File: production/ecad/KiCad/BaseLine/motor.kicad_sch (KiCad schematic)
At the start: 20 parts, among them J1 VibeMotorConnector_1, J8 VibeMotorConnector_2, U1 DRV8830DGQR, U10 DRV8830DGQR

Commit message: footprint stuff
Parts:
- R53, R54: value R_US -> 10k
- TP23, TP24: footprint TestPoint:TestPoint_2Pads_Pitch2.54mm_Drill0.8mm -> (none)
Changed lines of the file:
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@@
 			)
 		)
-		(property "Footprint" "TestPoint:TestPoint_2Pads_Pitch2.54mm_Drill0.8mm"
+		(property "Footprint" ""
 			(at 264.16 48.26 0)
 			(effects
@@
 			)
 		)
-		(property "Footprint" "TestPoint:TestPoint_2Pads_Pitch2.54mm_Drill0.8mm"
+		(property "Footprint" ""
 			(at 264.16 110.49 0)
 			(effects
@@
 			)
 		)
-		(property "Value" "R_US"
+		(property "Value" "10k"
 			(at 219.71 101.6 90)
 			(effects
@@
 			)
 		)
-		(property "Value" "R_US"
+		(property "Value" "10k"
 			(at 218.44 39.37 90)
 			(effects

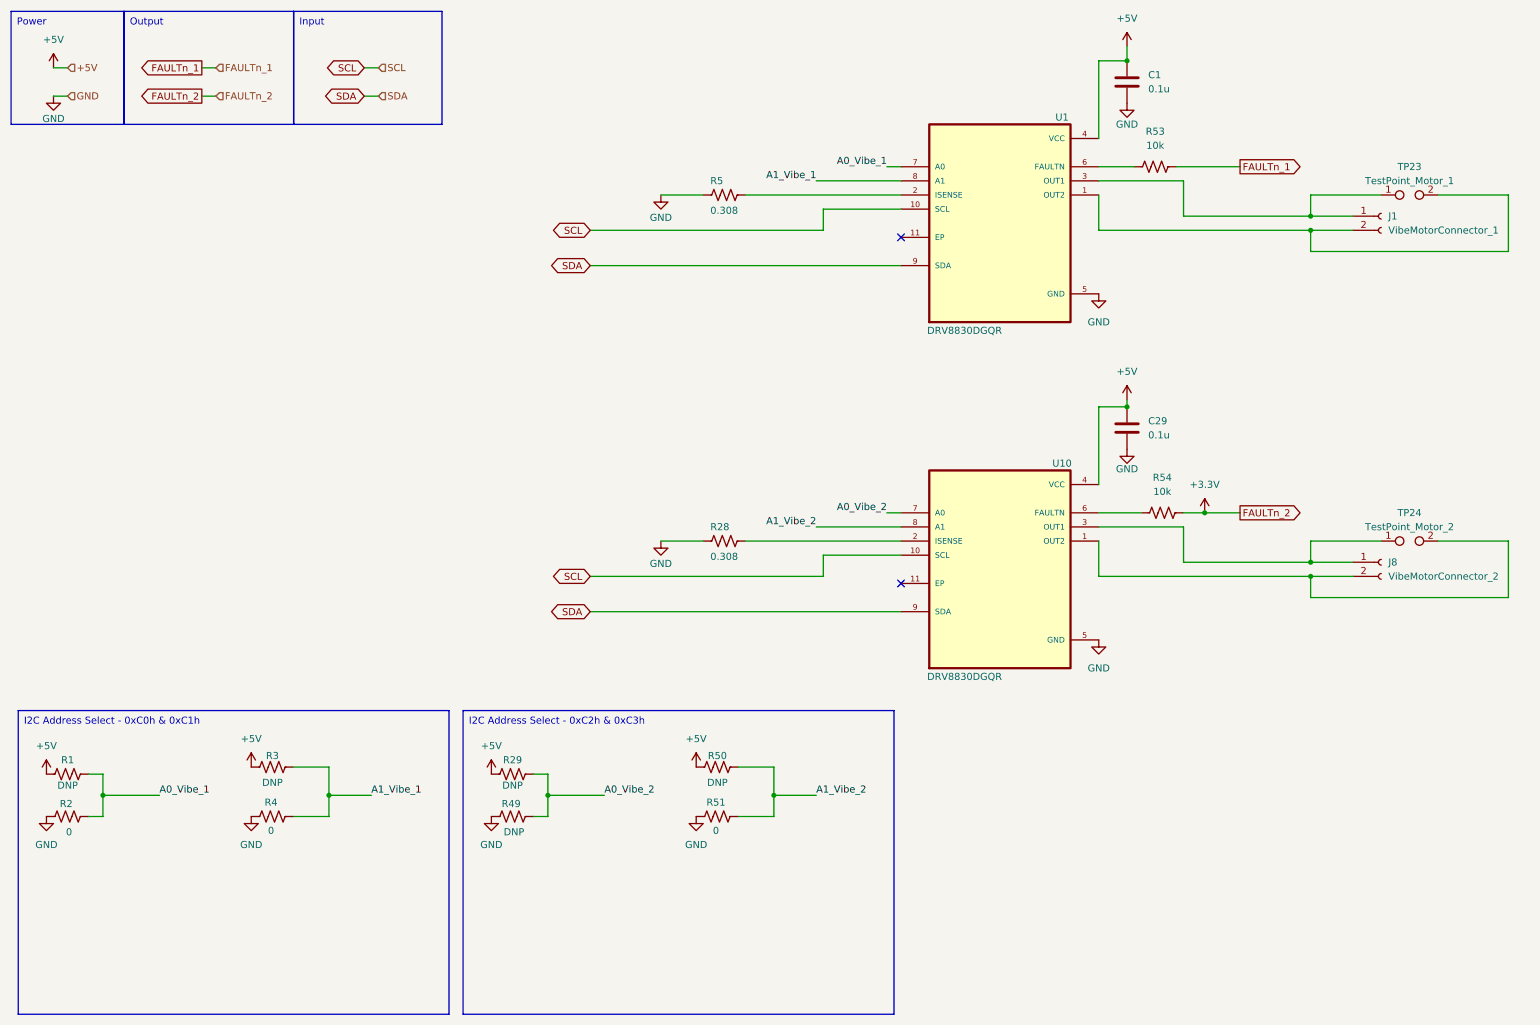
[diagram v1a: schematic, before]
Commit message: Connectors and heirarchal labels
added connectors for power on the Loadcell schem and the battery schem

added the MCU heirarchal labels
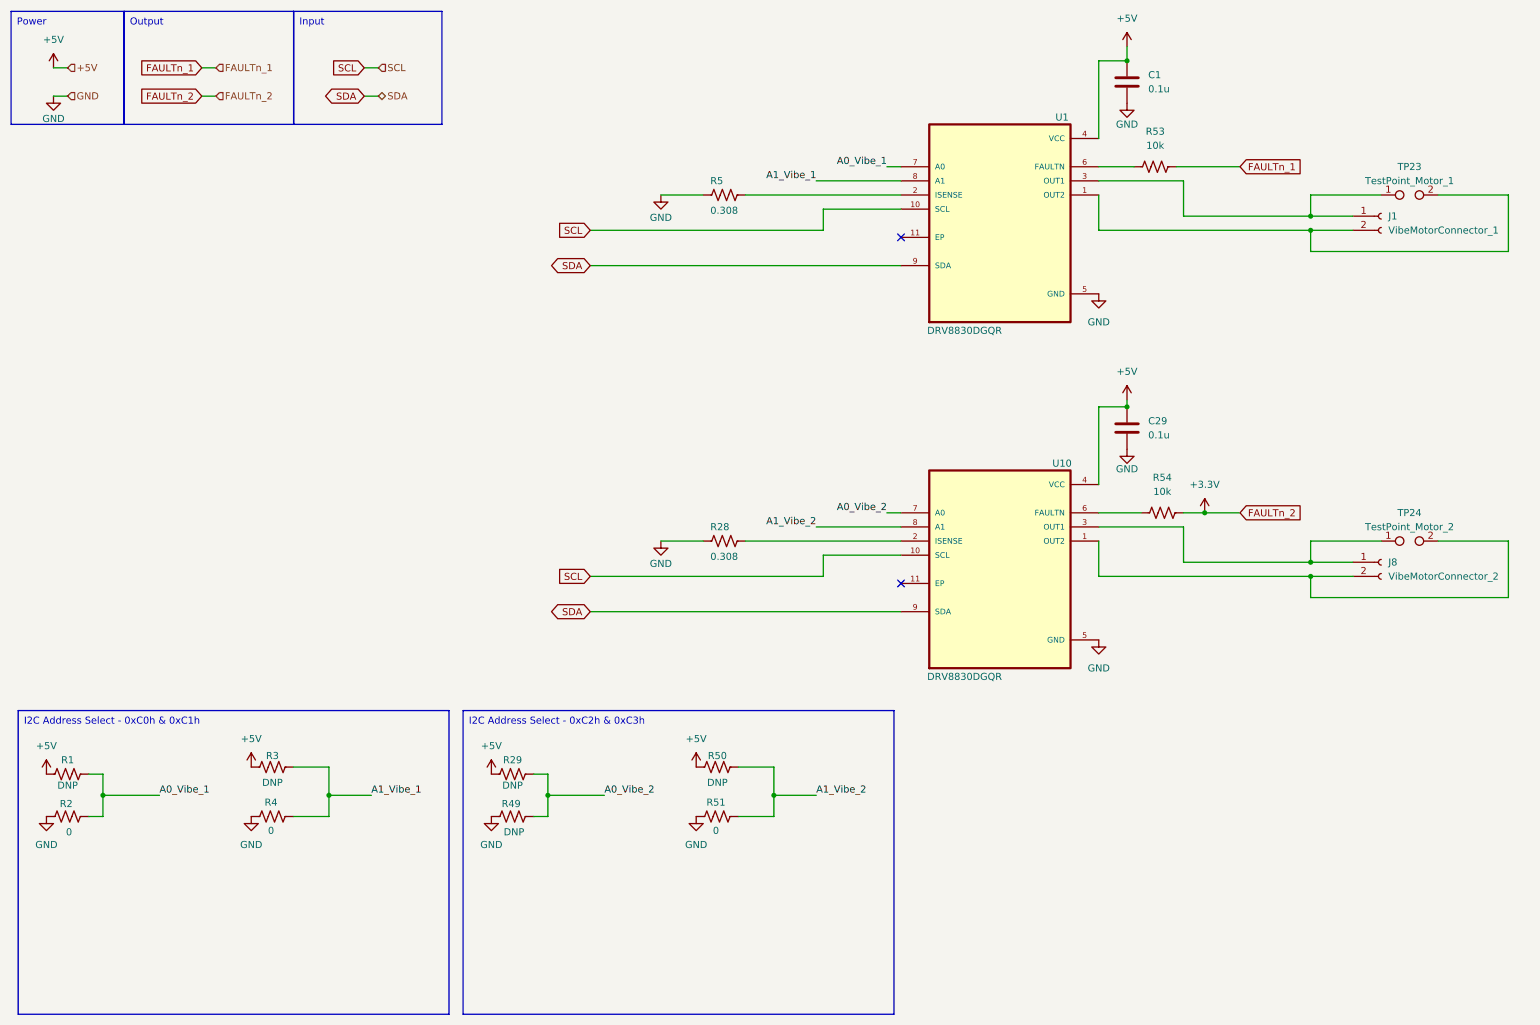
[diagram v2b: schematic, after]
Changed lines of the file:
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@@
 	)
 	(global_label "FAULTn_2"
-		(shape output)
+		(shape input)
 		(at 46.99 30.48 180)
 		(fields_autoplaced yes)
@@
 	)
 	(global_label "FAULTn_1"
-		(shape output)
+		(shape input)
 		(at 233.68 43.18 0)
 		(fields_autoplaced yes)
@@
 	)
 	(global_label "FAULTn_2"
-		(shape output)
+		(shape input)
 		(at 233.68 105.41 0)
 		(fields_autoplaced yes)
@@
 	)
 	(global_label "FAULTn_1"
-		(shape output)
+		(shape input)
 		(at 46.99 25.4 180)
 		(fields_autoplaced yes)
@@
 	)
 	(global_label "SCL"
-		(shape bidirectional)
+		(shape input)
 		(at 116.84 116.84 180)
 		(fields_autoplaced yes)
@@
 		)
 		(property "Intersheetrefs" "${INTERSHEET_REFS}"
-			(at 109.2359 116.84 0)
+			(at 110.3472 116.84 0)
 			(effects
 				(font
@@
 	)
 	(global_label "SCL"
-		(shape bidirectional)
+		(shape input)
 		(at 76.2 25.4 180)
 		(fields_autoplaced yes)
@@
 		)
 		(property "Intersheetrefs" "${INTERSHEET_REFS}"
-			(at 68.5959 25.4 0)
+			(at 69.7072 25.4 0)
 			(effects
 				(font
@@
 	)
 	(global_label "SCL"
-		(shape bidirectional)
+		(shape input)
 		(at 116.84 54.61 180)
 		(fields_autoplaced yes)
@@
 		)
 		(property "Intersheetrefs" "${INTERSHEET_REFS}"
-			(at 109.2359 54.61 0)
+			(at 110.3472 54.61 0)
 			(effects
 				(font
@@
 	)
 	(hierarchical_label "SDA"
-		(shape input)
+		(shape bidirectional)
 		(at 78.74 30.48 0)
 		(fields_autoplaced yes)

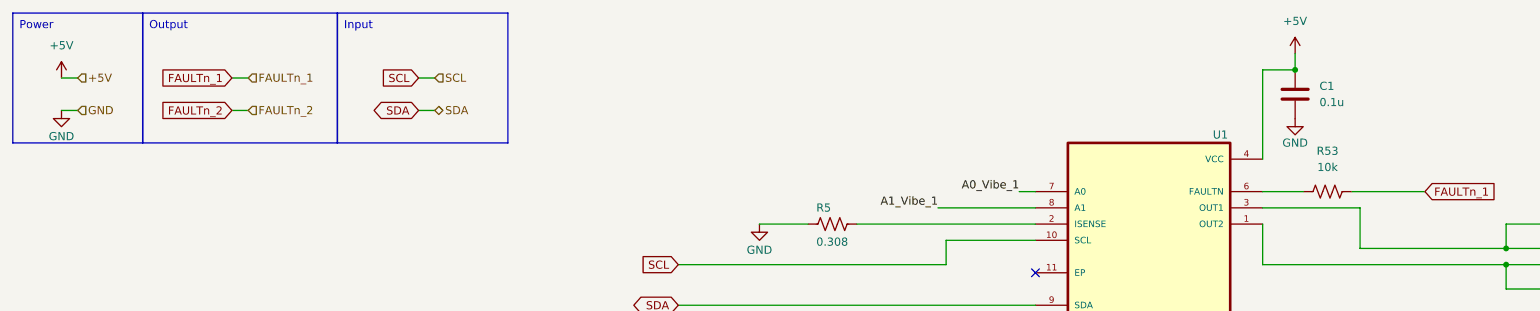
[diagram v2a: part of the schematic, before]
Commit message: fixed Faultn pull up to 3.3V
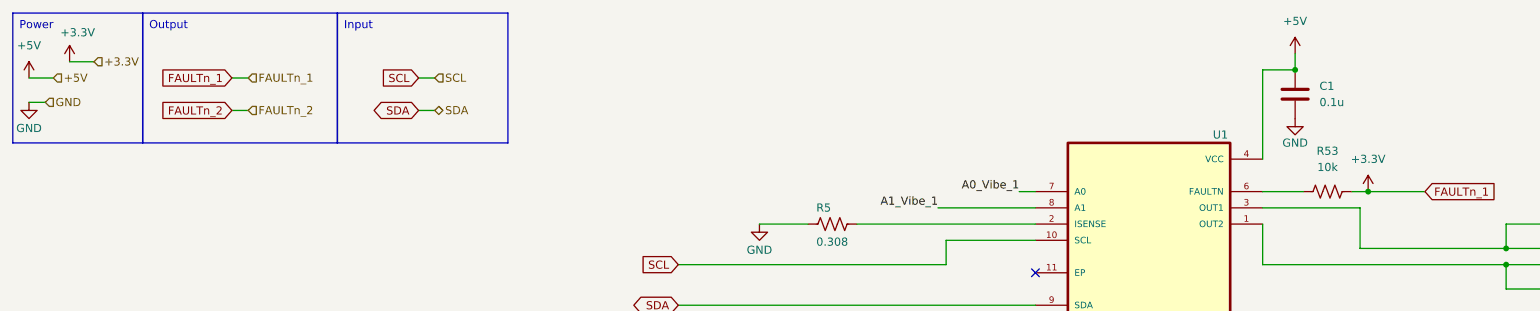
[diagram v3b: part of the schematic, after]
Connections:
- net FAULTn_1 is gone; now on net +3.3V: R53.2
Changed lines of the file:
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@@
 	)
 	(junction
+		(at 224.79 43.18)
+		(diameter 0)
+		(color 0 0 0 0)
+	)
+	(junction
 		(at 213.36 24.13)
 		(diameter 0)
@@
 	(wire
 		(pts
+			(xy 21.59 22.86) (xy 25.4 22.86)
+		)
+		(stroke
+			(width 0)
+			(type default)
+		)
+	)
+	(wire
+		(pts
 			(xy 109.22 152.4) (xy 106.68 152.4)
 		)
@@
 	(wire
 		(pts
-			(xy 20.32 25.4) (xy 22.86 25.4)
+			(xy 15.24 25.4) (xy 19.05 25.4)
 		)
 		(stroke
@@
 	(wire
 		(pts
+			(xy 224.79 43.18) (xy 233.68 43.18)
+		)
+		(stroke
+			(width 0)
+			(type default)
+		)
+	)
+	(wire
+		(pts
 			(xy 106.68 160.02) (xy 109.22 160.02)
 		)
@@
 	(wire
 		(pts
-			(xy 20.32 30.48) (xy 22.86 30.48)
+			(xy 15.24 29.21) (xy 17.78 29.21)
 		)
 		(stroke
@@
 	(wire
 		(pts
-			(xy 222.25 43.18) (xy 233.68 43.18)
+			(xy 222.25 43.18) (xy 224.79 43.18)
 		)
 		(stroke
@@
 	(hierarchical_label "GND"
 		(shape input)
-		(at 22.86 30.48 0)
+		(at 17.78 29.21 0)
 		(fields_autoplaced yes)
 		(effects
@@
 	(hierarchical_label "+5V"
 		(shape input)
-		(at 22.86 25.4 0)
+		(at 19.05 25.4 0)
+		(fields_autoplaced yes)
+		(effects
+			(font
+				(size 1.27 1.27)
+			)
+			(justify left)
+		)
+	)
+	(hierarchical_label "+3.3V"
+		(shape input)
+		(at 25.4 22.86 0)
 		(fields_autoplaced yes)
 		(effects
@@
 	(symbol
 		(lib_id "power:GND")
-		(at 20.32 30.48 0)
+		(at 15.24 29.21 0)
 		(unit 1)
 		(exclude_from_sim no)
@@
 		(dnp no)
 		(property "Reference" "#PWR092"
-			(at 20.32 36.83 0)
+			(at 15.24 35.56 0)
 			(effects
 				(font
@@
 		)
 		(property "Value" "GND"
-			(at 20.32 34.544 0)
+			(at 15.24 33.274 0)
 			(effects
 				(font
@@
 		)
 		(property "Footprint" ""
-			(at 20.32 30.48 0)
+			(at 15.24 29.21 0)
 			(effects
 				(font
@@
 		)
 		(property "Datasheet" ""
-			(at 20.32 30.48 0)
+			(at 15.24 29.21 0)
 			(effects
 				(font
@@
 		)
 		(property "Description" "Power symbol creates a global label with name \"GND\" , ground"
-			(at 20.32 30.48 0)
+			(at 15.24 29.21 0)
 			(effects
 				(font
@@
 	(symbol
 		(lib_id "power:+5V")
-		(at 20.32 25.4 0)
+		(at 15.24 25.4 0)
 		(unit 1)
 		(exclude_from_sim no)
@@
 		(fields_autoplaced yes)
 		(property "Reference" "#PWR091"
-			(at 20.32 29.21 0)
+			(at 15.24 29.21 0)
 			(effects
 				(font
@@
 		)
 		(property "Value" "+5V"
-			(at 20.32 20.32 0)
+			(at 15.24 20.32 0)
 			(effects
 				(font
@@
 		)
 		(property "Footprint" ""
-			(at 20.32 25.4 0)
+			(at 15.24 25.4 0)
 			(effects
 				(font
@@
 		)
 		(property "Datasheet" ""
-			(at 20.32 25.4 0)
+			(at 15.24 25.4 0)
 			(effects
 				(font
@@
 		)
 		(property "Description" "Power symbol creates a global label with name \"+5V\""
-			(at 20.32 25.4 0)
+			(at 15.24 25.4 0)
 			(effects
 				(font
@@
 	)
 	(symbol
+		(lib_id "power:+3.3V")
+		(at 224.79 43.18 0)
+		(unit 1)
+		(exclude_from_sim no)
+		(in_bom yes)
+		(on_board yes)
+		(dnp no)
+		(fields_autoplaced yes)
+		(property "Reference" "#PWR0121"
+			(at 224.79 46.99 0)
+			(effects
+				(font
+					(size 1.27 1.27)
+				)
+				(hide yes)
+			)
+		)
+		(property "Value" "+3.3V"
+			(at 224.79 38.1 0)
+			(effects
+				(font
+					(size 1.27 1.27)
+				)
+			)
+		)
+		(property "Footprint" ""
+			(at 224.79 43.18 0)
+			(effects
+				(font
+					(size 1.27 1.27)
+				)
+				(hide yes)
+			)
+		)
+		(property "Datasheet" ""
+			(at 224.79 43.18 0)
+			(effects
+				(font
+					(size 1.27 1.27)
+				)
+				(hide yes)
+			)
+		)
+		(property "Description" "Power symbol creates a global label with name \"+3.3V\""
+			(at 224.79 43.18 0)
+			(effects
+				(font
+					(size 1.27 1.27)
+				)
+				(hide yes)
+			)
+		)
+		(pin "1"
+		)
+		(instances
+			(project "BaseLine"
+				(path "/ba9eda21-3882-41e1-8265-3d8ac781da20/32bcaf69-2ff4-46a9-8a42-fce7269397e2"
+					(reference "#PWR0121")
+					(unit 1)
+				)
+			)
+		)
+	)
+	(symbol
 		(lib_id "Device:R_US")
 		(at 140.97 110.49 270)
@@
 					(unit 1)
 				)
+			)
+		)
+	)
+	(symbol
+		(lib_id "power:+3.3V")
+		(at 21.59 22.86 0)
+		(unit 1)
+		(exclude_from_sim no)
+		(in_bom yes)
+		(on_board yes)
+		(dnp no)
+		(property "Reference" "#PWR0122"
+			(at 21.59 26.67 0)
+			(effects
+				(font
+					(size 1.27 1.27)
+				)
+				(hide yes)
+			)
+		)
+		(property "Value" "+3.3V"
+			(at 22.86 18.288 0)
+			(effects
+				(font
+					(size 1.27 1.27)
+				)
+			)
+		)
+		(property "Footprint" ""
+			(at 21.59 22.86 0)
+			(effects
+				(font
+					(size 1.27 1.27)
+				)
+				(hide yes)
+			)
+		)
+		(property "Datasheet" ""
+			(at 21.59 22.86 0)
+			(effects
+				(font
+					(size 1.27 1.27)
+				)
+				(hide yes)
+			)
+		)
+		(property "Description" "Power symbol creates a global label with name \"+3.3V\""
+			(at 21.59 22.86 0)
+			(effects
+				(font
+					(size 1.27 1.27)
+				)
+				(hide yes)
+			)
+		)
+		(pin "1"
+		)
+		(instances
+			(project "BaseLine"
+				(path "/ba9eda21-3882-41e1-8265-3d8ac781da20/32bcaf69-2ff4-46a9-8a42-fce7269397e2"
+					(reference "#PWR0122")
+					(unit 1)
+				)

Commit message: Test point footprints changed
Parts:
- TP23, TP24: footprint (none) -> TestPoint:TestPoint_2Pads_Pitch2.54mm_Drill0.8mm
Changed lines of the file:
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@@
 			)
 		)
-		(property "Footprint" ""
+		(property "Footprint" "TestPoint:TestPoint_2Pads_Pitch2.54mm_Drill0.8mm"
 			(at 264.16 48.26 0)
 			(effects
@@
 			)
 		)
-		(property "Footprint" ""
+		(property "Footprint" "TestPoint:TestPoint_2Pads_Pitch2.54mm_Drill0.8mm"
 			(at 264.16 110.49 0)
 			(effects

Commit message: Fixed main footprint problems
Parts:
- J1: footprint BLT:JST_B2B-XH-A -> JST_B2B-XH-A:JST_B2B-XH-A
- J8: footprint BLT:JST_B2B-XH-A -> CONN_B4B-XH-AM_JST:CONN_B4B-XH-AM_JST
- U1: footprint DRV8830DGQR:IC_XTR111AIDGQR -> CONN_B4B-XH-AM_JST:CONN_B4B-XH-AM_JST
- U10: footprint DRV8830DGQR:IC_XTR111AIDGQR -> IC_XTR111AIDGQR:IC_XTR111AIDGQR
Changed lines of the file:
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@@
 			)
 		)
-		(property "Footprint" "DRV8830DGQR:IC_XTR111AIDGQR"
+		(property "Footprint" "IC_XTR111AIDGQR:IC_XTR111AIDGQR"
 			(at 190.5 115.57 0)
 			(effects
@@
 			)
 		)
-		(property "Footprint" "DRV8830DGQR:IC_XTR111AIDGQR"
+		(property "Footprint" "CONN_B4B-XH-AM_JST:CONN_B4B-XH-AM_JST"
 			(at 190.5 53.34 0)
 			(effects
@@
 			)
 		)
-		(property "Footprint" "BLT:JST_B2B-XH-A"
+		(property "Footprint" "JST_B2B-XH-A:JST_B2B-XH-A"
 			(at 259.08 52.07 0)
 			(effects
@@
 			)
 		)
-		(property "Footprint" "BLT:JST_B2B-XH-A"
+		(property "Footprint" "CONN_B4B-XH-AM_JST:CONN_B4B-XH-AM_JST"
 			(at 259.08 114.3 0)
 			(effects

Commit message: More footprint fixes
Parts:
- U1: footprint CONN_B4B-XH-AM_JST:CONN_B4B-XH-AM_JST -> IC_XTR111AIDGQR:IC_XTR111AIDGQR
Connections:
- net GND: now also U1.11 (EP), U10.11 (EP)
- no-connect marks 2 -> 0
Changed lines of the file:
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@@
 		(color 0 0 0 0)
 	)
-	(no_connect
-		(at 172.72 118.11)
-	)
-	(no_connect
-		(at 172.72 55.88)
-	)
 	(wire
 		(pts
@@
 	)
 	(symbol
+		(lib_id "power:GND")
+		(at 172.72 55.88 0)
+		(unit 1)
+		(exclude_from_sim no)
+		(in_bom yes)
+		(on_board yes)
+		(dnp no)
+		(property "Reference" "#PWR027"
+			(at 172.72 62.23 0)
+			(effects
+				(font
+					(size 1.27 1.27)
+				)
+				(hide yes)
+			)
+		)
+		(property "Value" "GND"
+			(at 172.72 59.436 0)
+			(effects
+				(font
+					(size 1.27 1.27)
+				)
+			)
+		)
+		(property "Footprint" ""
+			(at 172.72 55.88 0)
+			(effects
+				(font
+					(size 1.27 1.27)
+				)
+				(hide yes)
+			)
+		)
+		(property "Datasheet" ""
+			(at 172.72 55.88 0)
+			(effects
+				(font
+					(size 1.27 1.27)
+				)
+				(hide yes)
+			)
+		)
+		(property "Description" "Power symbol creates a global label with name \"GND\" , ground"
+			(at 172.72 55.88 0)
+			(effects
+				(font
+					(size 1.27 1.27)
+				)
+				(hide yes)
+			)
+		)
+		(pin "1"
+		)
+		(instances
+			(project "BaseLine"
+				(path "/ba9eda21-3882-41e1-8265-3d8ac781da20/32bcaf69-2ff4-46a9-8a42-fce7269397e2"
+					(reference "#PWR027")
+					(unit 1)
+				)
+			)
+		)
+	)
+	(symbol
 		(lib_id "DRV8830DGQR:DRV8830DGQR")
 		(at 190.5 115.57 0)
@@
 			)
 		)
-		(property "Footprint" "CONN_B4B-XH-AM_JST:CONN_B4B-XH-AM_JST"
+		(property "Footprint" "IC_XTR111AIDGQR:IC_XTR111AIDGQR"
 			(at 190.5 53.34 0)
 			(effects
@@
 					(unit 1)
 				)
+			)
+		)
+	)
+	(symbol
+		(lib_id "power:GND")
+		(at 172.72 118.11 0)
+		(unit 1)
+		(exclude_from_sim no)
+		(in_bom yes)
+		(on_board yes)
+		(dnp no)
+		(property "Reference" "#PWR028"
+			(at 172.72 124.46 0)
+			(effects
+				(font
+					(size 1.27 1.27)
+				)
+				(hide yes)
+			)
+		)
+		(property "Value" "GND"
+			(at 172.466 121.92 0)
+			(effects
+				(font
+					(size 1.27 1.27)
+				)
+			)
+		)
+		(property "Footprint" ""
+			(at 172.72 118.11 0)
+			(effects
+				(font
+					(size 1.27 1.27)
+				)
+				(hide yes)
+			)
+		)
+		(property "Datasheet" ""
+			(at 172.72 118.11 0)
+			(effects
+				(font
+					(size 1.27 1.27)
+				)
+				(hide yes)
+			)
+		)
+		(property "Description" "Power symbol creates a global label with name \"GND\" , ground"
+			(at 172.72 118.11 0)
+			(effects
+				(font
+					(size 1.27 1.27)
+				)
+				(hide yes)
+			)
+		)
+		(pin "1"
+		)
+		(instances
+			(project "BaseLine"
+				(path "/ba9eda21-3882-41e1-8265-3d8ac781da20/32bcaf69-2ff4-46a9-8a42-fce7269397e2"
+					(reference "#PWR028")
+					(unit 1)
+				)

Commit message: Fixed I/O mux select pins
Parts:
- J8: footprint CONN_B4B-XH-AM_JST:CONN_B4B-XH-AM_JST -> JST_B2B-XH-A:JST_B2B-XH-A
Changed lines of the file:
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@@
 			)
 		)
-		(property "Footprint" "CONN_B4B-XH-AM_JST:CONN_B4B-XH-AM_JST"
+		(property "Footprint" "JST_B2B-XH-A:JST_B2B-XH-A"
 			(at 259.08 114.3 0)
 			(effects

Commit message: added cp2102 footprint
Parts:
- J8: footprint JST_B2B-XH-A:JST_B2B-XH-A -> CONN_B4B-XH-AM_JST:CONN_B4B-XH-AM_JST
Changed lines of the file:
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@@
 			)
 		)
-		(property "Footprint" "JST_B2B-XH-A:JST_B2B-XH-A"
+		(property "Footprint" "CONN_B4B-XH-AM_JST:CONN_B4B-XH-AM_JST"
 			(at 259.08 114.3 0)
 			(effects
